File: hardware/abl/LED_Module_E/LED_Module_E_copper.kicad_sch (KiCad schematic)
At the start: 39 parts, among them K1 Conn_01x01, K10 Conn_01x01, K11 Conn_01x01, K12 Conn_01x01, K13 Conn_01x01, K14 Conn_01x01, K15 Conn_01x01, K16 Conn_01x01, K17 Conn_01x01, K18 Conn_01x01, K2 Conn_01x01, K3 Conn_01x01, K4 Conn_01x01, K5 Conn_01x01, K6 Conn_01x01, K7 Conn_01x01, K8 Conn_01x01, K9 Conn_01x01, U1 TMP1075DGK

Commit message: Many small adjustments for the next production run.
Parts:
- D1: value XEGAVT-H0-0000-000-000000K2001 -> XEGAWT-H2-0000-000-00000UT122G; Color (none) -> White 2200K; LCSC Part # (none) -> C9900154351; Manufacturer_Part_Number XEGAVT-H0-0000-000-000000K2001 -> XEGAWT-H2-0000-000-00000UT122G
- D11: value XEGAVT-H0-0000-000-000000K2001 -> XEGAWT-H2-0000-000-00000UT227H; Color (none) -> White 2700K; Manufacturer_Part_Number XEGAVT-H0-0000-000-000000K2001 -> XEGAWT-H2-0000-000-00000UT227H
- D12: value XEGAVT-H0-0000-000-000000K2001 -> XEGAAM-H2-0000-000-000000Q5001; Color (none) -> Amber; Manufacturer_Part_Number XEGAVT-H0-0000-000-000000K2001 -> XEGAAM-H2-0000-000-000000Q5001
- D2: value XEGAVT-H0-0000-000-000000K2001 -> XEGAAM-H2-0000-000-000000R4001; Color (none) -> Amber; Manufacturer_Part_Number XEGAVT-H0-0000-000-000000K2001 -> XEGAAM-H2-0000-000-000000R4001
- D3: value XEGAVT-H0-0000-000-000000K2001 -> XEGAPB-H0-0000-000-000000Q5001; Color (none) -> Poly Blue; LCSC Part # (none) -> C17674483; Manufacturer_Part_Number XEGAVT-H0-0000-000-000000K2001 -> XEGAPB-H0-0000-000-000000Q5001
- D4: value XEGAVT-H0-0000-000-000000K2001 -> XEGAWT-H2-0000-000-00000UT650G; Color (none) -> White 6500K; Manufacturer_Part_Number XEGAVT-H0-0000-000-000000K2001 -> XEGAWT-H2-0000-000-00000UT650G
- D5: value XEGAVT-H0-0000-000-000000K2001 -> XEGAPA-H0-0000-000-000000T3001; Color (none) -> Poly Amber; Manufacturer_Part_Number XEGAVT-H0-0000-000-000000K2001 -> XEGAPA-H0-0000-000-000000T3001
- D6: value XEGAVT-H0-0000-000-000000K2001 -> XEGAPL-H0-0000-000-000000V3001; Color (none) -> Poly Lime; LCSC Part # (none) -> C7545082; Manufacturer_Part_Number XEGAVT-H0-0000-000-000000K2001 -> XEGAPL-H0-0000-000-000000V3001
- D7: value XEGAVT-H0-0000-000-000000K2001 -> XEGAWT-H2-0000-000-00000UT330G; Color (none) -> White 3300K; LCSC Part # (none) -> C17192303; Manufacturer_Part_Number XEGAVT-H0-0000-000-000000K2001 -> XEGAWT-H2-0000-000-00000UT330G
- D8: value XEGAVT-H0-0000-000-000000K2001 -> XEGAPO-H0-0000-000-000000S3001; Color (none) -> Poly Red-Orange; LCSC Part # (none) -> C17313665; Manufacturer_Part_Number XEGAVT-H0-0000-000-000000K2001 -> XEGAPO-H0-0000-000-000000S3001
- H5, H6, LOGO1, TP1, TP2, TP3, TP4, TP5, TP6: now not fitted
- K1, K10, K11, K12, K13, K14, K15, K16, K17, K18, K2, K3, K4, K5, K6, K7, K8, K9: footprint TestPoint:TestPoint_THTPad_1.0x1.0mm_Drill0.5mm -> TestPoint:TestPoint_THTPad_D1.5mm_Drill0.7mm; now not fitted
- U1: footprint Package_SO:VSSOP-8_3.0x3.0mm_P0.65mm -> Package_SON:WSON-8-1EP_2x2mm_P0.5mm_EP0.9x1.6mm

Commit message: Add missing LCSC part numbers and bump version / date.
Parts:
- D11: value XEGAWT-H2-0000-000-00000UT227H -> XEGAWT-H2-0000-000-00000UT227H; LCSC Part # (none) -> C17584961
- D12: LCSC Part # (none) -> C17491029
- D2: LCSC Part # (none) -> C20921043
- D4: LCSC Part # (none) -> C17684059
- D5: LCSC Part # (none) -> C5438899
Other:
- title: besteLampe! LED Module F -> besteLampe! LED Module G
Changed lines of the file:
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@@
 	(paper "A4")
 	(title_block
-		(title "besteLampe! LED Module F")
-		(date "2024-11-12")
-		(rev "1.0")
+		(title "besteLampe! LED Module G")
+		(date "2024-11-28")
+		(rev "1.1")
 		(comment 1 "See  https://lenaschimmel.de/besteLampe! for the source and more information")
 		(comment 2 "This source describes Open Hardware and is licensed under the CERN-OHL-S v2.")
@@
 			)
 		)
+		(property "LCSC Part #" "C17491029"
+			(at 39.37 127 0)
+			(effects
+				(font
+					(size 1.27 1.27)
+				)
+				(hide yes)
+			)
+		)
 		(pin "2"
 		)
@@
 			)
 		)
+		(property "LCSC Part #" "C20921043"
+			(at 39.37 38.1 0)
+			(effects
+				(font
+					(size 1.27 1.27)
+				)
+				(hide yes)
+			)
+		)
 		(pin "2"
 		)
@@
 			)
 		)
+		(property "LCSC Part #" "C17684059"
+			(at 39.37 63.5 0)
+			(effects
+				(font
+					(size 1.27 1.27)
+				)
+				(hide yes)
+			)
+		)
 		(pin "2"
 		)
@@
 			)
 		)
-		(property "Value" "XEGAWT-H2-0000-000-00000UT227H "
+		(property "Value" "XEGAWT-H2-0000-000-00000UT227H"
 			(at 50.8 135.255 0)
 			(effects
@@
 			)
 		)
+		(property "LCSC Part #" "C17584961"
+			(at 39.37 139.7 0)
+			(effects
+				(font
+					(size 1.27 1.27)
+				)
+				(hide yes)
+			)
+		)
 		(pin "2"
 		)
@@
 			(at 39.37 76.2 0)
 			(effects
+				(font
+					(size 1.27 1.27)
+				)
+				(hide yes)
+			)
+		)
+		(property "LCSC Part #" "C5438899"
+			(at 39.37 76.2 0)
+			(effects

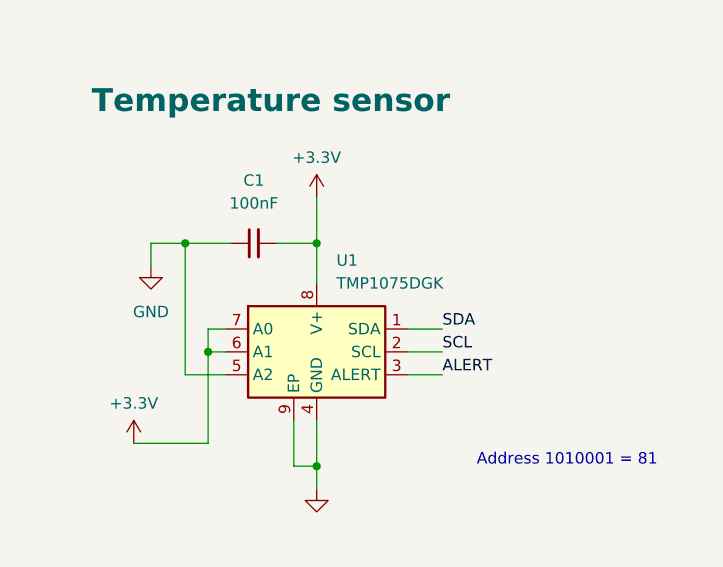
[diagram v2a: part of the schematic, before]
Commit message: Update files and documentation for LED modules E and G.
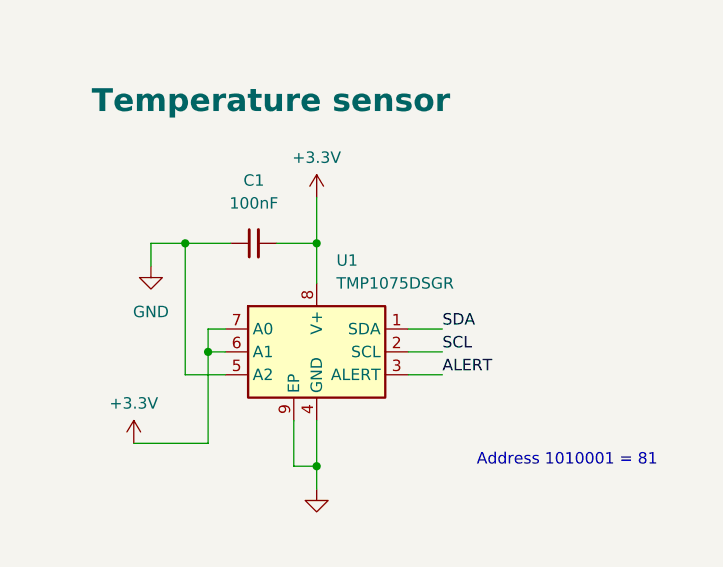
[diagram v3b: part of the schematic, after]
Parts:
- D1, D11, D12, D2, D3, D4, D5, D6, D7, D8: footprint Cree XLAMP XE-G LED XEGAVT-H0:XEGAVTH_clean -> Cree XLAMP XE-G LED XEGAVT-H0:XEGAVTH_PCBA
- U1: value TMP1075DGK -> TMP1075DSGR; LCSC Part # C2864807 -> C2870250; Manufacturer_Part_Number TMP1075DGKR -> TMP1075DSGR
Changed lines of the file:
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@@
 	(title_block
 		(title "besteLampe! LED Module G")
-		(date "2024-11-28")
+		(date "2024-12-01")
 		(rev "1.1")
 		(comment 1 "See  https://lenaschimmel.de/besteLampe! for the source and more information")
@@
 			)
 		)
-		(property "Value" "TMP1075DGK"
+		(property "Value" "TMP1075DSGR"
 			(at 202.8541 53.34 0)
 			(effects
@@
 			)
 		)
-		(property "Manufacturer_Part_Number" "TMP1075DGKR"
+		(property "Manufacturer_Part_Number" "TMP1075DSGR"
 			(at 200.66 60.96 0)
 			(effects
@@
 			)
 		)
-		(property "LCSC Part #" "C2864807"
+		(property "LCSC Part #" "C2870250"
 			(at 200.66 60.96 0)
 			(effects
@@
 			)
 		)
-		(property "Footprint" "Cree XLAMP XE-G LED XEGAVT-H0:XEGAVTH_clean"
+		(property "Footprint" "Cree XLAMP XE-G LED XEGAVT-H0:XEGAVTH_PCBA"
 			(at 58.42 124.46 0)
 			(effects
@@
 			)
 		)
-		(property "Footprint" "Cree XLAMP XE-G LED XEGAVT-H0:XEGAVTH_clean"
+		(property "Footprint" "Cree XLAMP XE-G LED XEGAVT-H0:XEGAVTH_PCBA"
 			(at 58.42 86.36 0)
 			(effects
@@
 			)
 		)
-		(property "Footprint" "Cree XLAMP XE-G LED XEGAVT-H0:XEGAVTH_clean"
+		(property "Footprint" "Cree XLAMP XE-G LED XEGAVT-H0:XEGAVTH_PCBA"
 			(at 58.42 99.06 0)
 			(effects
@@
 			)
 		)
-		(property "Footprint" "Cree XLAMP XE-G LED XEGAVT-H0:XEGAVTH_clean"
+		(property "Footprint" "Cree XLAMP XE-G LED XEGAVT-H0:XEGAVTH_PCBA"
 			(at 58.42 22.86 0)
 			(effects
@@
 			)
 		)
-		(property "Footprint" "Cree XLAMP XE-G LED XEGAVT-H0:XEGAVTH_clean"
+		(property "Footprint" "Cree XLAMP XE-G LED XEGAVT-H0:XEGAVTH_PCBA"
 			(at 58.42 35.56 0)
 			(effects
@@
 			)
 		)
-		(property "Footprint" "Cree XLAMP XE-G LED XEGAVT-H0:XEGAVTH_clean"
+		(property "Footprint" "Cree XLAMP XE-G LED XEGAVT-H0:XEGAVTH_PCBA"
 			(at 58.42 60.96 0)
 			(effects
@@
 			)
 		)
-		(property "Footprint" "Cree XLAMP XE-G LED XEGAVT-H0:XEGAVTH_clean"
+		(property "Footprint" "Cree XLAMP XE-G LED XEGAVT-H0:XEGAVTH_PCBA"
 			(at 58.42 48.26 0)
 			(effects
@@
 			)
 		)
-		(property "Footprint" "Cree XLAMP XE-G LED XEGAVT-H0:XEGAVTH_clean"
+		(property "Footprint" "Cree XLAMP XE-G LED XEGAVT-H0:XEGAVTH_PCBA"
 			(at 58.42 111.76 0)
 			(effects
@@
 			)
 		)
-		(property "Footprint" "Cree XLAMP XE-G LED XEGAVT-H0:XEGAVTH_clean"
+		(property "Footprint" "Cree XLAMP XE-G LED XEGAVT-H0:XEGAVTH_PCBA"
 			(at 58.42 137.16 0)
 			(effects
@@
 			)
 		)
-		(property "Footprint" "Cree XLAMP XE-G LED XEGAVT-H0:XEGAVTH_clean"
+		(property "Footprint" "Cree XLAMP XE-G LED XEGAVT-H0:XEGAVTH_PCBA"
 			(at 58.42 73.66 0)
 			(effects
